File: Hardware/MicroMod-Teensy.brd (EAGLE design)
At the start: 22 x 22.8 mm, 77 parts, among them J1 MICROMOD-2222, Q1 20V/4.2A/52mΩ/1.4W, Q2 20V/0.2A/8MHz/1.2Ω/1Vth, U1 IMXRT1062DV10X10, U2 W25QXX3X2, U3 MKL02Z32VFG4, Y1 32.768kHz, Y2 24MHz

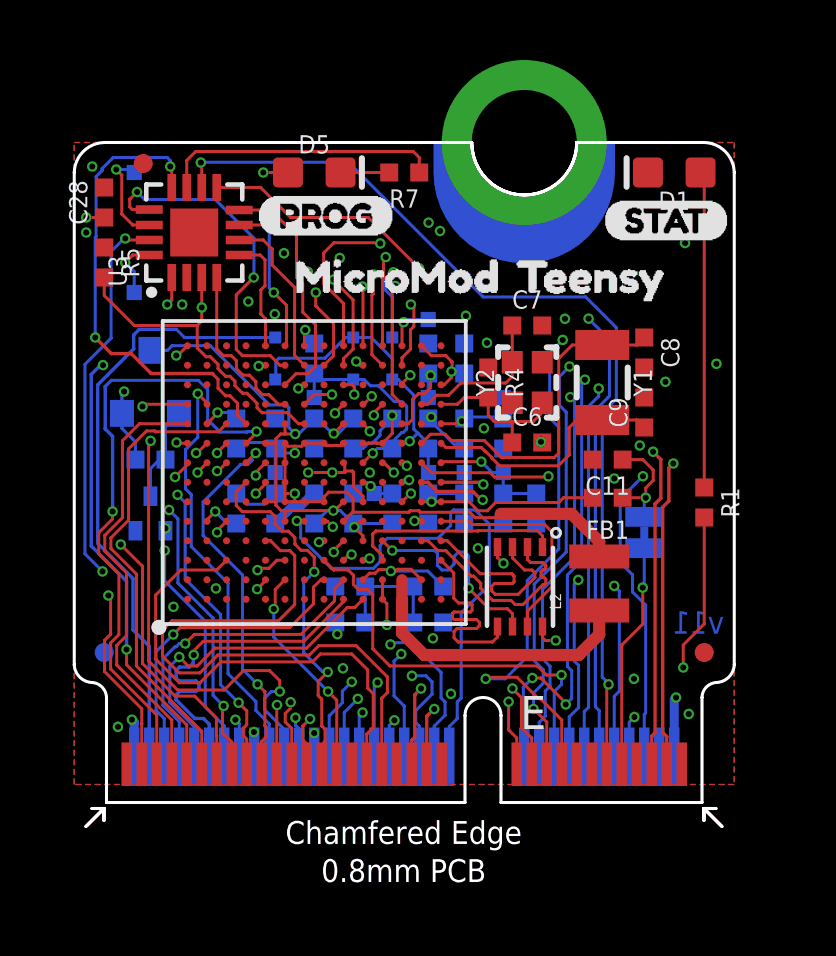
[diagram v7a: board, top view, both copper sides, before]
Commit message: Adding test point measurements
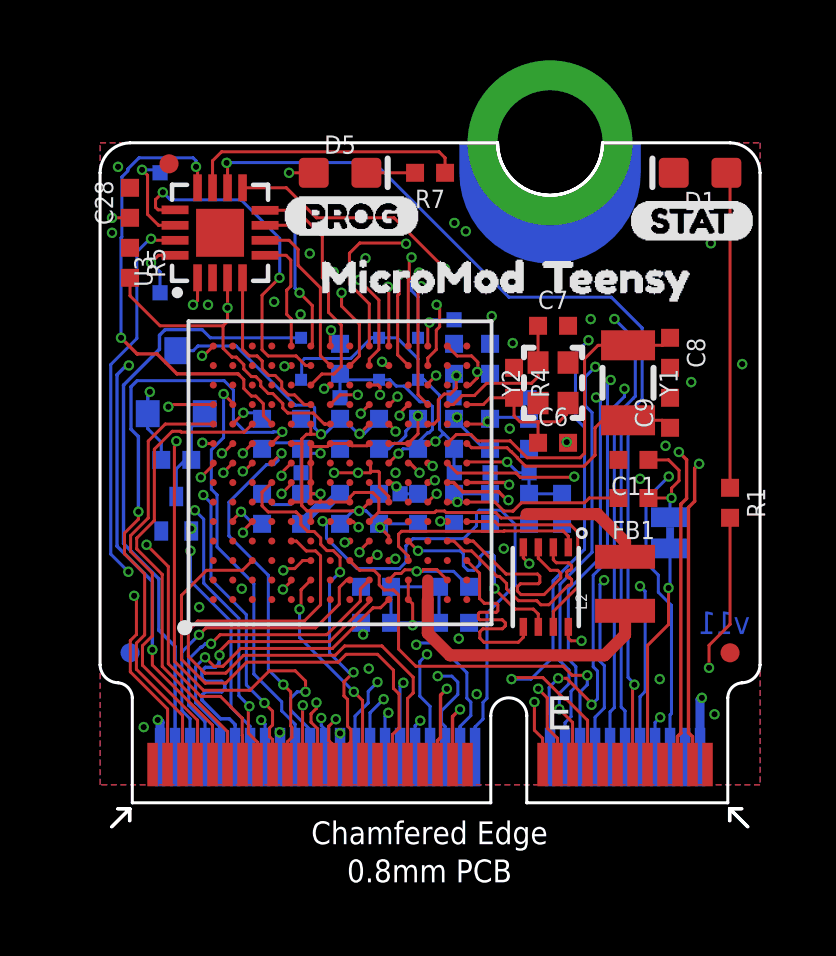
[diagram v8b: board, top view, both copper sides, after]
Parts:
- moved U$5 0.86 mm to (21.6, 15.5)
- moved U$6 0.86 mm to (17.6, 19.4)
- moved U$7 0.86 mm to (21.1, 6.59)
- moved Y1 0.86 mm to (17.6, 14.0)
- moved C1 0.86 mm to (9.30, 12.3)
- moved C10 0.86 mm to (11.8, 7.19)
- moved C13 0.86 mm to (11.8, 9.79)
- moved C14 0.86 mm to (11.8, 5.99)
- moved C22 0.86 mm to (11.8, 12.3)
- moved C23 0.86 mm to (11.8, 14.8)
- moved C25 0.86 mm to (14.3, 9.79)
- moved C26 0.86 mm to (14.3, 12.3)
- moved C27 0.86 mm to (15.4, 9.79)
- moved C5 0.86 mm to (9.30, 9.79)
- moved D4 0.86 mm to (9.30, 14.8)
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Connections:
- net N$1 renamed TP1
- net N$30 renamed TP5
- net N$33 renamed TP6
- net N$34 renamed TP7
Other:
- board text added: "All Test Point Measurements in mm"
- board text added: "TP is 0.5x0.5mm"
- board text added: "TP1"
- board text added: "TP10"
- board text added: "TP11"
- board text added: "TP2"
- board text added: "TP3"
- board text added: "TP4"
- board text added: "TP5"
- board text added: "TP6"
- board text added: "TP7"
- board text added: "TP8"
- board text added: "TP9"
- board text added: "Viewing Bottom of Board"
